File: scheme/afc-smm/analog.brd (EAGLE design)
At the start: 100 x 80 mm, 84 parts, among them IC1 OP1177R, IC10 LM2931-5.0, IC11 OP184, IC12 DAC8551, IC13 REF3033, IC14 317EMP, IC15 317EMP, IC2 TL082D, IC3 AD8515RJ, IC4 AD8615RJ, IC5 AD8221R, IC6 AD7476, IC7 REF3033, IC8 LM337LM, IC9 317EMP, J1 22-27-2031-03, J2 22-27-2021-02, Q1 IRLML2803, X1 1-227161-0, X2 1-227161-0

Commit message: commit before vocation
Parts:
- removed C15: (no value), rcl:C0603
- added C18, C19: (no value), rcl:SMC_A
- moved R24 333.2 mm to (41.6, 44.5), turned to 270 degrees
- moved R25 313.1 mm to (19.4, 28.3), turned to 90 degrees
- moved R13 291.2 mm to (40.0, 40.0), flipped to the bottom, turned to 90 degrees
- moved R15 290.7 mm to (55.9, 24.1), turned to 180 degrees
- moved R14 290.2 mm to (55.9, 27.0), turned to 180 degrees
- moved R12 287.3 mm to (38.1, 40.0), flipped to the bottom, turned to 90 degrees
- moved R10 267.7 mm to (14.9, 35.9), flipped to the bottom, turned to 90 degrees
- moved R11 262.7 mm to (11.7, 28.3), flipped to the bottom
- moved IC12 187.4 mm to (82.2, 9.53), flipped to the bottom
- moved R16 38.9 mm to (51.1, 29.8), flipped to the top, turned to 180 degrees
- moved C17 38.2 mm to (62.9, 37.5), flipped to the top, turned to 0 degrees
- moved R8 37.6 mm to (62.9, 34.9), flipped to the top
- moved R17 35.7 mm to (51.4, 33.7), turned to 180 degrees
- moved R9 33.8 mm to (62.9, 39.7), flipped to the top, turned to 0 degrees
- moved IC7 32.5 mm to (57.5, 40.3), flipped to the top, turned to 270 degrees
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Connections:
- removed net N$14: IC1.2, R13.1, R24.1
- net +3.3V: now also C18.+, R19.2
- net GND: now also C18.-, C19.-
- net N$13: now also IC1.2, R13.1, R24.1
- net N$27: now also C19.+; no longer C15.2
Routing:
- net GND: track 152.2 -> 202.4 mm, vias 0 -> 1
- net -12V: track 13.0 -> 58.5 mm, vias 0 -> 1
- net N$29: track 3.95 -> 41.1 mm, vias 0 -> 1
- net +3.3V: track 3.76 -> 31.7 mm, vias 0 -> 2
- net N$9: track 0.00 -> 22.7 mm, vias 0 -> 1
- net N$2: track 0.00 -> 19.7 mm, vias 0 -> 1
- net +12V: track 25.3 -> 44.4 mm
- net N$27: track 0.00 -> 17.6 mm, vias 0 -> 1
- net N$13: track 0.00 -> 16.5 mm
- net N$15: track 0.00 -> 14.4 mm
- net N$17: track 0.00 -> 13.8 mm
- net N$19: track 0.00 -> 11.0 mm
- net N$1: track 0.00 -> 10.2 mm
- net N$5: track 0.00 -> 7.83 mm
- net +5V: track 9.98 -> 16.2 mm
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
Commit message: make analog in, not compleate yet
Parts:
- moved R27 413.1 mm to (74.0, 50.2), turned to 90 degrees
- moved R26 411.6 mm to (77.5, 50.2), turned to 90 degrees
- moved LED2 409.7 mm to (74.0, 54.9)
- moved LED1 408.5 mm to (77.5, 54.9)
- moved R11 20.7 mm to (22.9, 45.7), turned to 180 degrees
- moved R25 15.2 mm to (24.4, 42.5)
- moved SV1 6.73 mm to (74.9, 30.2)
- moved Q1 5.68 mm to (46.0, 29.2), flipped to the bottom, turned to 0 degrees
- moved R15 5.48 mm to (54.9, 29.5)
- moved R14 4.55 mm to (54.9, 31.4)
- moved R4 4.26 mm to (21.9, 56.5), turned to 180 degrees
- moved R16 3.14 mm to (53.3, 27.6), turned to 0 degrees
- moved C4 2.29 mm to (31.1, 60.0), turned to 90 degrees
- moved C7 2.13 mm to (27.3, 60.3), turned to 90 degrees
- moved R5 1.00 mm to (21.9, 58.7)
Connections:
- new net N$16: LED1.A, R26.2
- net GND: now also LED1.C, LED2.C
- net N$20: now also LED2.A, R27.2; no longer R11.2
- net N$29: now also R11.2
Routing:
- net +12V: track 44.4 -> 99.3 mm, vias 0 -> 1
- net GND: track 202.4 -> 251.1 mm, vias 1 -> 3
- net +5V: track 16.2 -> 35.3 mm
- net N$29: track 41.1 -> 54.2 mm
- net N$5: track 7.83 -> 16.6 mm, vias 0 -> 1
- net N$2: track 19.7 -> 12.3 mm, vias 1 -> 0
- net N$17: track 13.8 -> 10.5 mm
- net N$18: track 0.00 -> 3.22 mm
- net N$19: track 11.0 -> 13.8 mm
- net N$24: track 5.66 -> 8.27 mm
- net N$8: track 0.00 -> 1.91 mm
- net -12V: track 58.5 -> 59.9 mm, vias 1 -> 2
- net N$13: track 16.5 -> 17.0 mm

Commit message: make analog out schematics, draw most of brd
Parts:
- added D4, D5: 1N4148WS, afc-smm:SOD323
- C14: device rcl:C0603 -> rcl:SMC_A
- SV1: device con-lstb:MA08-2W -> con-lstb:MA10-2W
- X1, X2: device con-coax:AMP_227161 -> afc-smm:AMP_227161
- moved B2 334.5 mm to (25.7, 5.40), flipped to the bottom, turned to 270 degrees
- moved C12 331.6 mm to (68.6, 4.45), flipped to the bottom, turned to 270 degrees
- moved C14 329.5 mm to (32.4, 17.8), flipped to the bottom, turned to 180 degrees
- moved R23 303.9 mm to (24.4, 25.7), flipped to the bottom, turned to 180 degrees
- moved R22 301.2 mm to (21.0, 27.6), flipped to the bottom
- moved R20 298.3 mm to (66.0, 9.53), flipped to the bottom, turned to 90 degrees
- moved R21 296.9 mm to (66.0, 4.45), flipped to the bottom, turned to 90 degrees
- moved R6 246.2 mm to (47.0, 9.84), flipped to the bottom, turned to 90 degrees
- moved R7 245.2 mm to (47.0, 4.45), flipped to the bottom, turned to 90 degrees
- moved C11 221.6 mm to (71.4, 4.76), turned to 270 degrees
- moved C13 206.0 mm to (35.6, 5.40), turned to 270 degrees
- moved TP9 204.3 mm to (69.2, 12.1)
- moved C10 204.1 mm to (50.2, 4.45), flipped to the bottom, turned to 270 degrees
- moved C9 201.9 mm to (53.3, 4.76), turned to 270 degrees
- moved TP11 195.8 mm to (31.8, 25.1)
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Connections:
- removed net REF: IC12.2
- removed net VDD: IC12.1
- new net N$14: IC6.4, SV1.1
- new net N$21: IC6.5, SV1.3
- new net N$22: IC6.6, SV1.5
- new net N$23: B2.AC1, J2.2
- new net N$26: R27.1, SV1.2
- new net N$31: B2.+, C13.+, D4.1, IC14.3
- new net N$32: C11.+, C12.1, D5.2, IC13.1, IC15.4, R20.2, TP9.TP
- new net N$33: IC14.1, R6.1, R7.2
- new net N$34: C10.1, C9.+, D4.2, D5.1, IC11.7, IC14.4, IC15.3, R6.2, TP8.TP
- new net N$37: IC15.1, R20.1, R21.2
- new net N$39: C14.+, IC12.1, IC12.2, IC13.2, TP10.TP
- new net N$40: IC12.6, SV1.11
- new net N$41: IC11.6, R22.2, TP12.TP, X2.1
- new net N$42: IC12.7, SV1.13
- new net N$44: IC11.2, R22.1, R23.2
- new net N$45: IC12.5, SV1.9
- new net N$47: IC11.3, IC12.3, IC12.4, TP11.TP
- new net N$51: B2.AC2, J2.1
- new net N$7: R26.1, SV1.4
- net GND: now also B2.-, C10.2, C11.-, C12.2, C13.-, C14.-, C9.-, IC11.4, IC13.3, R21.1, R23.1, R7.1, SV1.17, SV1.18, X2.2
- net N$8: now also SV1.7
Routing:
- net GND: track 251.1 -> 354.3 mm
- net N$32: track 0.00 -> 45.6 mm
- net N$45: track 0.00 -> 38.7 mm
- net N$40: track 0.00 -> 38.2 mm
- net N$42: track 0.00 -> 38.0 mm
- net N$34: track 0.00 -> 28.0 mm
- net +12V: track 99.3 -> 123.1 mm
- net N$8: track 1.91 -> 18.5 mm
- net N$3: track 37.7 -> 21.4 mm
- net N$41: track 0.00 -> 15.4 mm
- net N$51: track 0.00 -> 15.4 mm
- net N$39: track 0.00 -> 14.5 mm
- net N$22: track 0.00 -> 14.5 mm
- net N$14: track 0.00 -> 14.2 mm
- net N$21: track 0.00 -> 14.1 mm
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
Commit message: compleat? version 0.1 first
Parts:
- added JP1: (no value), afc-smm:1X01
- added S1: (no value), switch-omron:B3F-10XX
- R24, R25: device rcl:RTRIM3296W -> afc-smm:RTRIM3296W
- SV1: device con-lstb:MA10-2W -> afc-smm:MA10-2W
- moved R25 17.5 mm to (41.9, 51.4), turned to 270 degrees
- moved R24 17.2 mm to (24.4, 53.3), turned to 90 degrees
- moved R11 10.2 mm to (33.0, 53.0)
- moved TP8 9.53 mm to (43.8, 10.2), flipped to the bottom
- moved TP7 8.41 mm to (51.1, 54.3), flipped to the bottom
- moved TP9 7.24 mm to (62.2, 10.2), flipped to the bottom
- moved R20 6.67 mm to (59.4, 9.53)
- moved R21 6.67 mm to (59.4, 4.45)
- moved C9 6.03 mm to (47.3, 4.76)
- moved C13 6.03 mm to (29.5, 5.40)
- moved D4 6.03 mm to (31.1, 10.5)
- moved C10 6.03 mm to (44.1, 4.45)
- moved C11 6.03 mm to (65.4, 4.76)
- moved C12 6.03 mm to (62.5, 4.45)
- moved D5 6.03 mm to (48.9, 9.21)
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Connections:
- new net N$55: S1.1, S1.2, SV1.6
- net GND: now also JP1.1, R24.1, S1.3, S1.4; no longer R25.1
- net N$13: now also R25.1, R25.2; no longer R24.1, R24.2
- net N$17: now also R24.2; no longer R25.2
- net N$18: now also R24.3; no longer R25.3
- net N$9: now also R25.3; no longer R24.3
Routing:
- net GND: track 354.3 -> 507.3 mm, vias 3 -> 6
- net N$34: track 28.0 -> 75.3 mm
- net N$55: track 0.00 -> 37.3 mm
- net N$7: track 0.00 -> 15.3 mm
- net N$26: track 0.00 -> 12.6 mm
- net N$29: track 54.2 -> 44.2 mm
- net N$18: track 3.22 -> 13.1 mm
- net N$47: track 5.53 -> 13.3 mm
- net N$51: track 15.4 -> 8.80 mm
- net +12V: track 123.1 -> 128.6 mm, vias 1 -> 2
- net N$32: track 45.6 -> 40.7 mm
- net N$41: track 15.4 -> 19.4 mm
- net N$38: track 21.9 -> 25.4 mm
- net N$44: track 12.3 -> 8.84 mm
- net N$8: track 18.5 -> 21.8 mm
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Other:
- board size 100 x 80 mm -> 80 x 80 mm

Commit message: little improvement after production
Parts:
- moved TP3 6.16 mm to (58.7, 60.6)
- moved R26 4.45 mm to (76.5, 48.9)
- moved R27 4.45 mm to (73.0, 48.9)
- moved LED1 4.13 mm to (76.5, 54.3)
- moved LED2 4.13 mm to (73.0, 54.3)
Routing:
- net N$7: track 15.3 -> 10.9 mm
- net N$26: track 12.6 -> 8.14 mm
- net +5V: track 31.0 -> 27.2 mm
- net GND: track 507.3 -> 504.8 mm
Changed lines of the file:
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@@
 <attribute name="TP_SIGNAL_NAME" value="" x="51.1175" y="77.47" size="1.778" layer="28" rot="MR270" display="off"/>
 </element>
-<element name="TP3" library="testpad" package="B2,54" value="TPSB2,54" x="63.8175" y="64.135" rot="MR0">
-<attribute name="TP_SIGNAL_NAME" value="" x="63.8175" y="64.135" size="1.778" layer="28" rot="MR0" display="off"/>
+<element name="TP3" library="testpad" package="B2,54" value="TPSB2,54" x="58.7375" y="60.6425" rot="MR0">
+<attribute name="TP_SIGNAL_NAME" value="" x="58.7375" y="60.6425" size="1.778" layer="28" rot="MR0" display="off"/>
 </element>
 <element name="TP4" library="testpad" package="B2,54" value="TPSB2,54" x="55.88" y="49.8475" rot="MR0">
@@
 <element name="B1" library="rectifier" package="DBS" value="DBS101G" x="16.1925" y="67.31" rot="MR270"/>
 <element name="B2" library="rectifier" package="DBS" value="DBS101G" x="22.225" y="5.3975" rot="MR270"/>
-<element name="LED1" library="led" package="CHIPLED_0805" value="" x="76.5175" y="58.42"/>
-<element name="LED2" library="led" package="CHIPLED_0805" value="" x="73.025" y="58.42"/>
-<element name="R26" library="rcl" package="R0603" value="" x="76.5175" y="53.34" rot="R90"/>
-<element name="R27" library="rcl" package="R0603" value="" x="73.025" y="53.34" rot="R90"/>
+<element name="LED1" library="led" package="CHIPLED_0805" value="" x="76.5175" y="54.2925"/>
+<element name="LED2" library="led" package="CHIPLED_0805" value="" x="73.025" y="54.2925"/>
+<element name="R26" library="rcl" package="R0603" value="" x="76.5175" y="48.895" rot="R90"/>
+<element name="R27" library="rcl" package="R0603" value="" x="73.025" y="48.895" rot="R90"/>
 <element name="C18" library="rcl" package="SMC_A" value="" x="55.245" y="35.56" rot="MR0"/>
 <element name="C19" library="rcl" package="SMC_A" value="" x="55.5625" y="45.085" rot="MR270"/>
@@
 <wire x1="41.275" y1="21.2725" x2="41.5925" y2="20.955" width="0.6096" layer="16"/>
 <via x="41.5925" y="20.955" extent="1-16" drill="0.8" diameter="1.9304"/>
-<wire x1="76.5175" y1="59.47" x2="73.025" y2="59.47" width="0.6096" layer="1"/>
+<wire x1="76.5175" y1="55.3425" x2="73.025" y2="55.3425" width="0.6096" layer="1"/>
 <wire x1="75.565" y1="20.6375" x2="73.025" y2="20.6375" width="0.6096" layer="16"/>
 <wire x1="73.025" y1="20.6375" x2="77.1525" y2="20.6375" width="0.6096" layer="16"/>
 <wire x1="77.1525" y1="20.6375" x2="78.4225" y2="21.9075" width="0.6096" layer="16"/>
-<wire x1="78.4225" y1="21.9075" x2="78.4225" y2="66.675" width="0.6096" layer="16"/>
-<wire x1="78.4225" y1="66.675" x2="77.7875" y2="67.31" width="0.6096" layer="16"/>
-<wire x1="77.7875" y1="67.31" x2="73.025" y2="67.31" width="0.6096" layer="16"/>
-<wire x1="73.025" y1="67.31" x2="72.7075" y2="66.9925" width="0.6096" layer="16"/>
-<wire x1="72.7075" y1="66.9925" x2="72.7075" y2="63.7794" width="0.6096" layer="16"/>
+<wire x1="78.4225" y1="21.9075" x2="78.4225" y2="56.8325" width="0.6096" layer="16"/>
 <wire x1="72.7075" y1="63.7794" x2="72.6694" y2="63.7413" width="0.6096" layer="16"/>
-<wire x1="72.6694" y1="70.2437" x2="72.6694" y2="67.0306" width="0.6096" layer="16"/>
-<wire x1="72.6694" y1="67.0306" x2="72.7075" y2="66.9925" width="0.6096" layer="16"/>
-<wire x1="72.6694" y1="63.7413" x2="72.6694" y2="59.8256" width="0.6096" layer="1"/>
-<wire x1="72.6694" y1="59.8256" x2="73.025" y2="59.47" width="0.6096" layer="1"/>
 <wire x1="16.1925" y1="74.92" x2="16.1925" y2="69.5325" width="1.27" layer="16"/>
 <wire x1="16.1925" y1="69.5325" x2="18.415" y2="67.31" width="1.27" layer="16"/>
@@
 <wire x1="42.8625" y1="68.2625" x2="47.625" y2="68.2625" width="0.6096" layer="16"/>
 <wire x1="42.545" y1="35.2425" x2="42.8625" y2="35.2425" width="0.6096" layer="16"/>
+<wire x1="72.7075" y1="63.7794" x2="72.6694" y2="63.7794" width="0.6096" layer="16"/>
+<wire x1="72.6694" y1="63.7794" x2="72.6694" y2="70.2437" width="0.6096" layer="16"/>
+<wire x1="78.4225" y1="56.8325" x2="72.6694" y2="62.5856" width="0.6096" layer="16"/>
+<wire x1="72.6694" y1="62.5856" x2="72.6694" y2="63.7413" width="0.6096" layer="16"/>
+<wire x1="73.025" y1="55.3425" x2="73.025" y2="63.3857" width="0.6096" layer="1"/>
+<wire x1="73.025" y1="63.3857" x2="72.6694" y2="63.7413" width="0.6096" layer="1"/>
 </signal>
 <signal name="N$1">
@@
 <wire x1="56.1975" y1="51.1175" x2="56.1975" y2="48.745" width="0.6096" layer="1"/>
 <wire x1="56.1975" y1="48.745" x2="56.3675" y2="48.575" width="0.6096" layer="1"/>
-<wire x1="59.3725" y1="63.5" x2="63.1825" y2="63.5" width="0.6096" layer="16"/>
-<wire x1="63.1825" y1="63.5" x2="63.8175" y2="64.135" width="0.6096" layer="16"/>
 <wire x1="59.3725" y1="63.5" x2="59.3725" y2="62.5475" width="0.6096" layer="16"/>
-<wire x1="59.3725" y1="62.5475" x2="55.88" y2="59.055" width="0.6096" layer="16"/>
+<wire x1="59.3725" y1="62.5475" x2="58.1025" y2="61.2775" width="0.6096" layer="16"/>
 <via x="55.88" y="59.055" extent="1-16" drill="0.8" diameter="1.9304"/>
+<wire x1="58.1025" y1="61.2775" x2="55.88" y2="59.055" width="0.6096" layer="16"/>
 <wire x1="55.88" y1="59.055" x2="55.88" y2="53.34" width="0.6096" layer="1"/>
 <wire x1="55.88" y1="53.34" x2="57.15" y2="52.07" width="0.6096" layer="1"/>
@@
 <wire x1="59.3725" y1="66.3575" x2="59.3725" y2="69.155" width="0.6096" layer="16"/>
 <wire x1="58.9525" y1="66.3575" x2="59.3725" y2="66.3575" width="0.6096" layer="16"/>
+<wire x1="58.7375" y1="60.6425" x2="58.1025" y2="61.2775" width="0.6096" layer="16"/>
 </signal>
 <signal name="N$30">
@@
 <contactref element="LED1" pad="A"/>
 <contactref element="R26" pad="2"/>
-<wire x1="76.5175" y1="54.19" x2="76.5175" y2="57.37" width="0.6096" layer="1"/>
+<wire x1="76.5175" y1="49.745" x2="76.5175" y2="53.2425" width="0.6096" layer="1"/>
 </signal>
 <signal name="N$20">
 <contactref element="LED2" pad="A"/>
 <contactref element="R27" pad="2"/>
-<wire x1="73.025" y1="54.19" x2="73.025" y2="57.37" width="0.6096" layer="1"/>
+<wire x1="73.025" y1="49.745" x2="73.025" y2="53.2425" width="0.6096" layer="1"/>
 </signal>
 <signal name="N$14">
@@
 <contactref element="R27" pad="1"/>
 <contactref element="SV1" pad="2"/>
-<wire x1="75.565" y1="40.9575" x2="75.565" y2="46.99" width="0.6096" layer="1"/>
-<wire x1="75.565" y1="46.99" x2="73.025" y2="49.53" width="0.6096" layer="1"/>
-<wire x1="73.025" y1="49.53" x2="73.025" y2="52.49" width="0.6096" layer="1"/>
+<wire x1="75.565" y1="40.9575" x2="75.565" y2="44.1325" width="0.6096" layer="1"/>
+<wire x1="75.565" y1="44.1325" x2="73.025" y2="46.6725" width="0.6096" layer="1"/>
+<wire x1="73.025" y1="46.6725" x2="73.025" y2="48.045" width="0.6096" layer="1"/>
 </signal>
 <signal name="N$7">
@@
 <wire x1="76.5175" y1="38.4175" x2="76.835" y2="38.4175" width="0.6096" layer="1"/>
 <wire x1="76.835" y1="38.4175" x2="77.7875" y2="39.37" width="0.6096" layer="1"/>
-<wire x1="77.7875" y1="39.37" x2="77.7875" y2="51.22" width="0.6096" layer="1"/>
-<wire x1="77.7875" y1="51.22" x2="76.5175" y2="52.49" width="0.6096" layer="1"/>
+<wire x1="77.7875" y1="39.37" x2="77.7875" y2="46.775" width="0.6096" layer="1"/>
+<wire x1="77.7875" y1="46.775" x2="76.5175" y2="48.045" width="0.6096" layer="1"/>
 <wire x1="75.565" y1="38.4175" x2="76.5175" y2="38.4175" width="0" layer="19" extent="1-1"/>
 </signal>

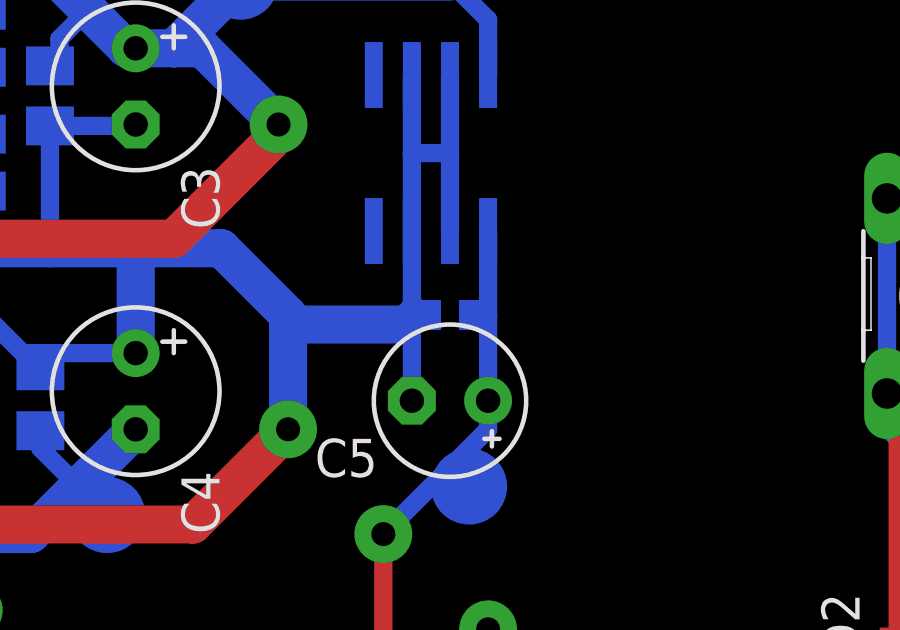
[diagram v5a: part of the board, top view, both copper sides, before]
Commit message: add component value
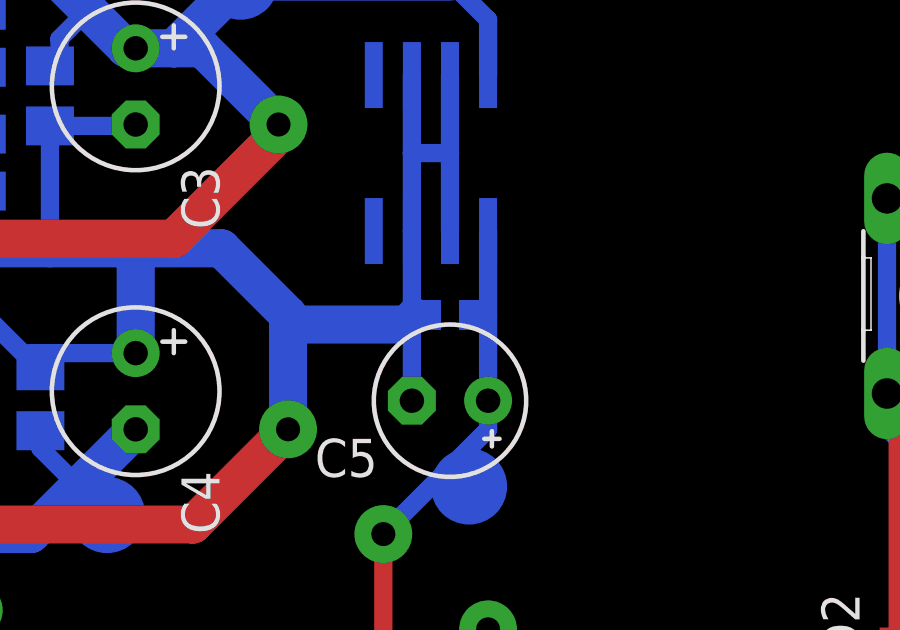
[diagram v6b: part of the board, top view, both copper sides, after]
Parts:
- C1, C11, C13, C2, C3, C4, C5, C9: value (none) -> 100u
- C10, C12, C16, C17, C6, C7, C8: value (none) -> 0.1
- C14, C18: value (none) -> 10u
- C19: value (none) -> 1.0u
- R1: value (none) -> 499
- R10: value (none) -> 1M
- R11: value (none) -> 750k
- R12, R13, R16, R23: value (none) -> 10k
- R14: value (none) -> 7k5
- R15: value (none) -> 3k
- R17, R24, R25, R8, R9: value (none) -> 100k
- R18: value (none) -> 2k
- R19: value (none) -> 10
- R2, R20, R5, R6: value (none) -> 240
- R21: value (none) -> 750
- R22: value (none) -> 75k
- R26, R27: value (none) -> 1k
- R3, R4: value (none) -> 2k2
- R7: value (none) -> 5k6
- X1, X2: value 1-227161-0 -> BNC-206
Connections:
- net +5V: now also C8.1; no longer C8.2
- net GND: now also C8.2; no longer C8.1
